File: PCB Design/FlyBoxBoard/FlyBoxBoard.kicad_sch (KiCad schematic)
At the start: 40 parts, among them J1 Screw_Terminal_01x02, J10 Screw_Terminal_01x02, J11 Screw_Terminal_01x02, J12 Screw_Terminal_01x02, J13 Screw_Terminal_01x02, J14 Conn_01x04_Female, J15 Conn_01x06_Female, J16 Conn_01x02_Female, J17 Conn_01x02_Female, J18 Conn_01x05_Female, J19 Conn_01x02_Female, J2 Screw_Terminal_01x02, J20 Conn_01x03_Female, J21 Conn_01x03_Female, J22 Conn_01x03_Female, J23 Conn_01x10_Female, J24 Conn_01x03_Female, J25 Conn_01x05_Female, J26 Conn_01x07_Female, J27 Conn_01x10_Female, J28 Conn_01x03_Female, J29 Conn_01x02_Female, J3 Conn_01x15_Female, J30 Conn_01x02_Female, J31 Conn_01x02_Female, J32 Conn_01x02_Female, J33 Conn_01x02_Female, J34 Conn_01x02_Female, J35 Conn_01x03_Female, J36 Conn_01x03_Female, J37 Conn_01x03_Female, J38 Conn_01x07_Female, J39 Conn_01x07_Female, J4 Conn_01x06_Female, J40 Conn_01x07_Female, J5 Conn_01x15_Female, J6 Conn_01x05_Female, J7 Conn_01x05_Female, J8 Conn_01x05_Female, J9 Screw_Terminal_01x04

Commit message: schematic now has no errors
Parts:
- J14: footprint (none) -> Connector_PinSocket_2.54mm:PinSocket_1x04_P2.54mm_Vertical
- J15: footprint (none) -> Connector_PinSocket_2.54mm:PinSocket_1x06_P2.54mm_Vertical
- J18, J6: footprint (none) -> Connector_PinSocket_2.54mm:PinSocket_1x05_P2.54mm_Vertical
- J19, J30: footprint (none) -> Connector_PinSocket_2.54mm:PinSocket_1x02_P2.54mm_Vertical
- J21, J35: footprint (none) -> Connector_PinSocket_2.54mm:PinSocket_1x03_P2.54mm_Vertical
- J23: footprint (none) -> Connector_PinSocket_2.54mm:PinSocket_1x10_P2.54mm_Vertical
- J38: footprint (none) -> Connector_PinSocket_2.54mm:PinSocket_1x07_P2.54mm_Vertical
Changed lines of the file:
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@@
       (effects (font (size 1.27 1.27)) (justify left))
     )
-    (property "Footprint" "" (id 2) (at 26.67 64.77 0)
+    (property "Footprint" "Connector_PinSocket_2.54mm:PinSocket_1x05_P2.54mm_Vertical" (id 2) (at 26.67 64.77 0)
       (effects (font (size 1.27 1.27)) hide)
     )
@@
       (effects (font (size 1.27 1.27)) (justify left))
     )
-    (property "Footprint" "" (id 2) (at 227.33 73.66 0)
+    (property "Footprint" "Connector_PinSocket_2.54mm:PinSocket_1x03_P2.54mm_Vertical" (id 2) (at 227.33 73.66 0)
       (effects (font (size 1.27 1.27)) hide)
     )
@@
       (effects (font (size 1.27 1.27)) (justify left))
     )
-    (property "Footprint" "" (id 2) (at 252.73 73.66 0)
+    (property "Footprint" "Connector_PinSocket_2.54mm:PinSocket_1x07_P2.54mm_Vertical" (id 2) (at 252.73 73.66 0)
       (effects (font (size 1.27 1.27)) hide)
     )
@@
       (effects (font (size 1.27 1.27)) (justify left))
     )
-    (property "Footprint" "" (id 2) (at 102.87 85.09 0)
+    (property "Footprint" "Connector_PinSocket_2.54mm:PinSocket_1x05_P2.54mm_Vertical" (id 2) (at 102.87 85.09 0)
       (effects (font (size 1.27 1.27)) hide)
     )
@@
       (effects (font (size 1.27 1.27)) (justify left))
     )
-    (property "Footprint" "" (id 2) (at 146.05 40.64 0)
+    (property "Footprint" "Connector_PinSocket_2.54mm:PinSocket_1x10_P2.54mm_Vertical" (id 2) (at 146.05 40.64 0)
       (effects (font (size 1.27 1.27)) hide)
     )
@@
       (effects (font (size 1.27 1.27)) (justify left))
     )
-    (property "Footprint" "" (id 2) (at 127 48.26 0)
+    (property "Footprint" "Connector_PinSocket_2.54mm:PinSocket_1x03_P2.54mm_Vertical" (id 2) (at 127 48.26 0)
       (effects (font (size 1.27 1.27)) hide)
     )
@@
       (effects (font (size 1.27 1.27)) (justify left))
     )
-    (property "Footprint" "" (id 2) (at 201.93 66.04 0)
+    (property "Footprint" "Connector_PinSocket_2.54mm:PinSocket_1x02_P2.54mm_Vertical" (id 2) (at 201.93 66.04 0)
       (effects (font (size 1.27 1.27)) hide)
     )
@@
       (effects (font (size 1.27 1.27)) (justify left))
     )
-    (property "Footprint" "" (id 2) (at 102.87 102.87 0)
+    (property "Footprint" "Connector_PinSocket_2.54mm:PinSocket_1x02_P2.54mm_Vertical" (id 2) (at 102.87 102.87 0)
       (effects (font (size 1.27 1.27)) hide)
     )
@@
       (effects (font (size 1.27 1.27)) (justify left))
     )
-    (property "Footprint" "" (id 2) (at 63.5 87.63 0)
+    (property "Footprint" "Connector_PinSocket_2.54mm:PinSocket_1x06_P2.54mm_Vertical" (id 2) (at 63.5 87.63 0)
       (effects (font (size 1.27 1.27)) hide)
     )
@@
       (effects (font (size 1.27 1.27)) (justify left))
     )
-    (property "Footprint" "" (id 2) (at 63.5 55.88 0)
-      (effects (font (size 1.27 1.27)) hide)
-    )
+    (property "Footprint" "Connector_PinSocket_2.54mm:PinSocket_1x04_P2.54mm_Vertical" (id 2) (at 63.5 55.88 0)
+      (effects (font (size 1.27 1.27)) hide)
+    )

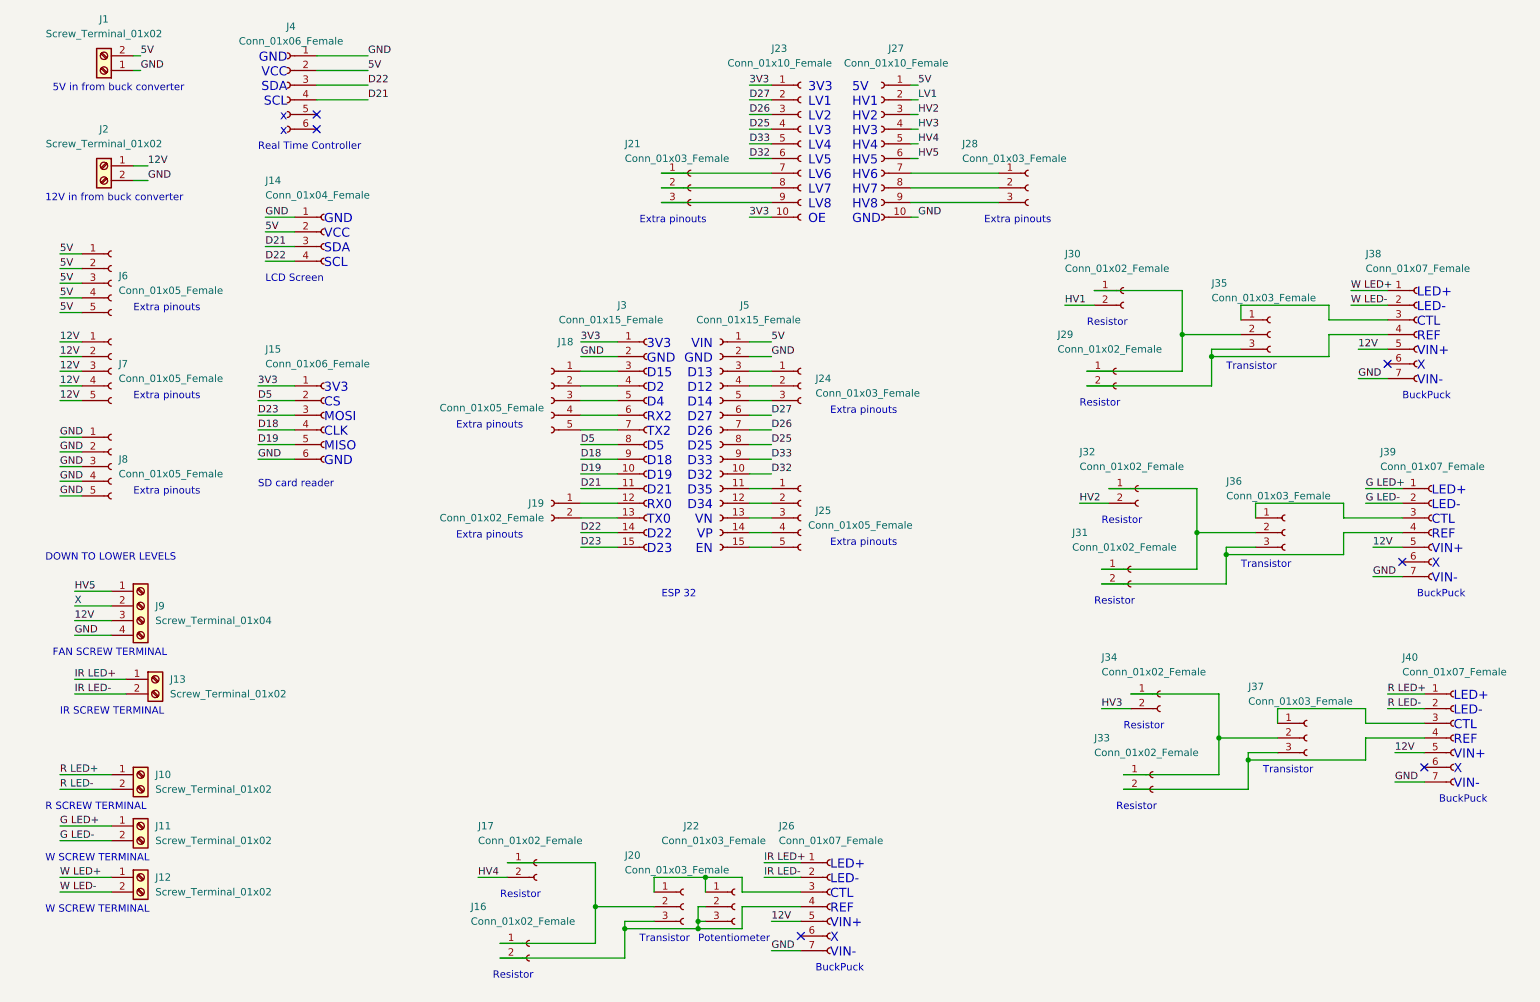
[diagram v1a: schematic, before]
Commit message: Labeling on components
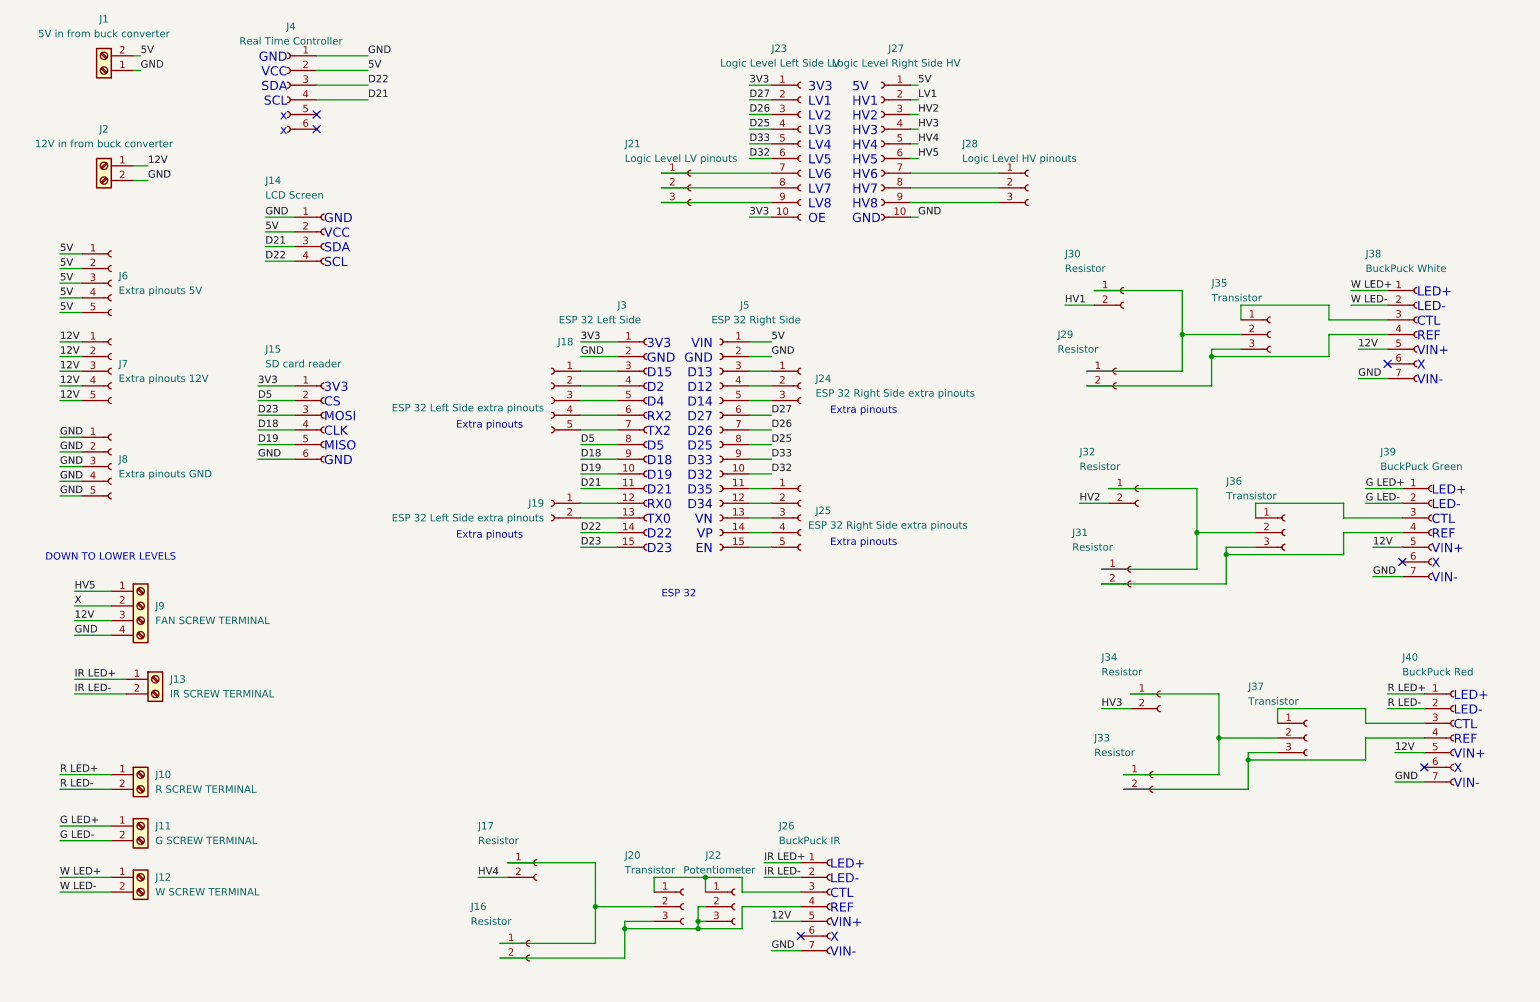
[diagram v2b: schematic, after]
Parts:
- J1: value Screw_Terminal_01x02 -> 5V in from buck converter
- J10: value Screw_Terminal_01x02 -> R SCREW TERMINAL
- J11: value Screw_Terminal_01x02 -> G SCREW TERMINAL
- J12: value Screw_Terminal_01x02 -> W SCREW TERMINAL
- J13: value Screw_Terminal_01x02 -> IR SCREW TERMINAL
- J14: value Conn_01x04_Female -> LCD Screen
- J15: value Conn_01x06_Female -> SD card reader
- J16, J17, J29, J30, J31, J32, J33, J34: value Conn_01x02_Female -> Resistor
- J18: value Conn_01x05_Female -> ESP 32 Left Side extra pinouts
- J19: value Conn_01x02_Female -> ESP 32 Left Side extra pinouts
- J2: value Screw_Terminal_01x02 -> 12V in from buck converter
- J20, J35, J36, J37: value Conn_01x03_Female -> Transistor
- J21: value Conn_01x03_Female -> Logic Level LV pinouts
- J22: value Conn_01x03_Female -> Potentiometer
- J23: value Conn_01x10_Female -> Logic Level Left Side LV
- J24: value Conn_01x03_Female -> ESP 32 Right Side extra pinouts
- J25: value Conn_01x05_Female -> ESP 32 Right Side extra pinouts
- J26: value Conn_01x07_Female -> BuckPuck IR
- J27: value Conn_01x10_Female -> Logic Level Right Side HV
- J28: value Conn_01x03_Female -> Logic Level HV pinouts
- J3: value Conn_01x15_Female -> ESP 32 Left Side
- J38: value Conn_01x07_Female -> BuckPuck White
- J39: value Conn_01x07_Female -> BuckPuck Green
- J4: value Conn_01x06_Female -> Real Time Controller
- J40: value Conn_01x07_Female -> BuckPuck Red
- J5: value Conn_01x15_Female -> ESP 32 Right Side
- J6: value Conn_01x05_Female -> Extra pinouts 5V
- J7: value Conn_01x05_Female -> Extra pinouts 12V
- J8: value Conn_01x05_Female -> Extra pinouts GND
- J9: value Screw_Terminal_01x04 -> FAN SCREW TERMINAL
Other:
- note removed: "12V in from buck converter"
- note removed: "5V in from buck converter"
- note removed: "BuckPuck"
- note removed: "FAN SCREW TERMINAL"
- note removed: "IR SCREW TERMINAL"
- note removed: "LCD Screen"
- note removed: "Potentiometer"
- note removed: "R SCREW TERMINAL"
- note removed: "Real Time Controller"
- note removed: "Resistor"
- note removed: "SD card reader"
- note removed: "Transistor"
- note removed: "W SCREW TERMINAL"

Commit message: PCB progress
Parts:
- J16, J17, J29, J30, J31, J32, J33, J34: footprint Connector_PinSocket_2.54mm:PinSocket_1x02_P2.54mm_Vertical -> Connector_PinSocket_2.54mm:PinSocket_1x05_P2.54mm_Vertical; symbol Connector:Conn_01x02_Female -> Connector:Conn_01x05_Female
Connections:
- net LV1 is gone; now on net HV1: J27.2 (Pin_2)
- net HV1: now also J30.5 (Pin_5); no longer J30.2 (Pin_2)
- net HV2: now also J32.5 (Pin_5); no longer J32.2 (Pin_2)
- net HV3: now also J34.5 (Pin_5); no longer J34.2 (Pin_2)
- net HV4: now also J17.5 (Pin_5); no longer J17.2 (Pin_2)
- net at J20.3 (Pin_3), J22.2 (Pin_2), J22.3 (Pin_3)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: now also J16.5 (Pin_5); no longer J16.2 (Pin_2)
- net at J35.3 (Pin_3), J38.4 (Pin_4): now also J29.5 (Pin_5); no longer J29.2 (Pin_2)
- net at J37.3 (Pin_3), J40.4 (Pin_4): now also J33.5 (Pin_5); no longer J33.2 (Pin_2)
- net at J36.3 (Pin_3), J39.4 (Pin_4): now also J31.5 (Pin_5); no longer J31.2 (Pin_2)
- no-connect marks 6 -> 30
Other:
- moved on the sheet: J35, J37, J38, J40

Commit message: 3/1 updates
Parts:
- J1: value 5V in from buck converter -> 5V in; footprint Connector_PinSocket_2.54mm:PinSocket_1x02_P2.54mm_Vertical -> TerminalBlock:TerminalBlock_bornier-2_P5.08mm
- J10: value R SCREW TERMINAL -> RED; footprint Connector_PinSocket_2.54mm:PinSocket_1x02_P2.54mm_Vertical -> TerminalBlock:TerminalBlock_bornier-2_P5.08mm
- J11: value G SCREW TERMINAL -> GREEN; footprint Connector_PinSocket_2.54mm:PinSocket_1x02_P2.54mm_Vertical -> TerminalBlock:TerminalBlock_bornier-2_P5.08mm
- J12: value W SCREW TERMINAL -> WHITE; footprint Connector_PinSocket_2.54mm:PinSocket_1x02_P2.54mm_Vertical -> TerminalBlock:TerminalBlock_bornier-2_P5.08mm
- J13: value IR SCREW TERMINAL -> INFRARED; footprint Connector_PinSocket_2.54mm:PinSocket_1x02_P2.54mm_Vertical -> TerminalBlock:TerminalBlock_bornier-2_P5.08mm
- J16, J17, J29, J30, J31, J32, J33, J34: value Resistor -> 5K Ohms
- J2: value 12V in from buck converter -> 12V in; footprint Connector_PinSocket_2.54mm:PinSocket_1x02_P2.54mm_Vertical -> TerminalBlock:TerminalBlock_bornier-2_P5.08mm
- J21: value Logic Level LV pinouts -> Logic Level LV pins
- J22: footprint Connector_PinSocket_2.54mm:PinSocket_1x03_P2.54mm_Vertical -> Connector_PinSocket_2.54mm:PinSocket_1x05_P2.54mm_Vertical; symbol Connector:Conn_01x03_Female -> Connector:Conn_01x05_Female
- J28: value Logic Level HV pinouts -> Logic Level HV pins
- J9: value FAN SCREW TERMINAL -> FANS
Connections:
- net D21: now also J4.3 (Pin_3); no longer J4.4 (Pin_4)
- net D22: now also J4.4 (Pin_4); no longer J4.3 (Pin_3)
- net at J20.1 (Pin_1), J22.1 (Pin_1), J26.3 (Pin_3): now also J22.3 (Pin_3)
- net at J16.5 (Pin_5), J20.3 (Pin_3), J26.4 (Pin_4): now also J22.5 (Pin_5); no longer J22.2 (Pin_2), J22.3 (Pin_3)
- no-connect marks 30 -> 32
